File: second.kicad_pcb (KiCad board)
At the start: 2 copper layers, 55 x 100 mm, 48 parts, among them J1 Conn_01x02_Socket, J10 Conn_01x02_Socket, J11 USB_C_Receptacle_USB2.0_16P, J12 Conn_01x03_Socket, J13 Conn_01x02_Socket, J14 Conn_01x02_Socket, J2 Conn_01x03_Socket, J3 Conn_01x03_Socket, J4 Conn_01x03_Socket, J5 Conn_01x03_Socket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

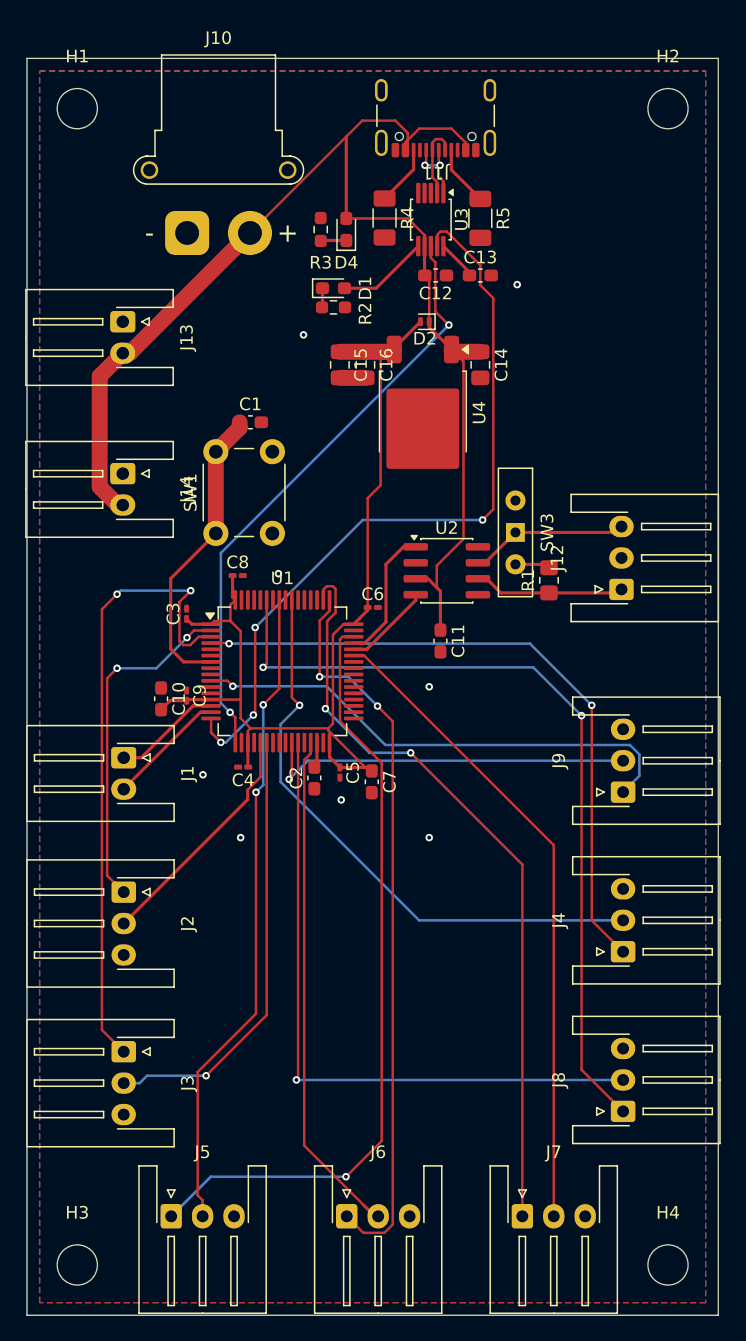
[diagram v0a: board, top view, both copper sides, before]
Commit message: DRCの実行、gndベタの最適化
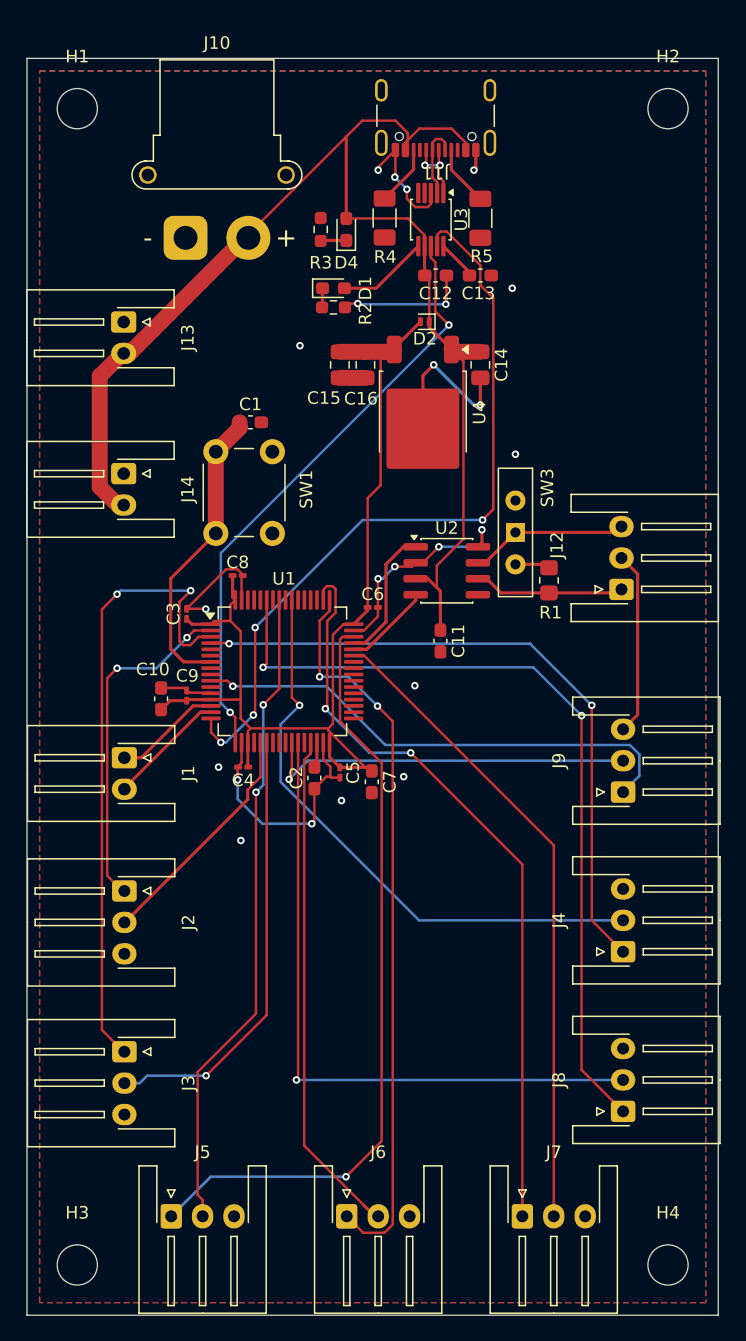
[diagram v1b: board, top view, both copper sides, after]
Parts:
- moved J10 0.41 mm to (62.6, 64.3)
- moved J2 0.10 mm to (57.7, 116.2)
- moved J13 0.07 mm to (57.7, 71.0)
- moved J14 0.07 mm to (57.7, 83.0)
- moved J3 0.05 mm to (57.7, 129.0)
- moved J1 0.05 mm to (57.7, 105.6)
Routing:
- net GND: track 2.03 -> 99.9 mm, vias 0 -> 23
- net (no net): vias 8 -> 0
